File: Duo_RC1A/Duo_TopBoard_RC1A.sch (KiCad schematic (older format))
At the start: 32 parts, among them CN1 CONN_PANNEL_2X2, CN2 CONN_PANNEL_2X2, P1 PIN_ARRAY_2X10, P2 KK3.96_2, Q1 MMBT3904, Q2 MMBT3904

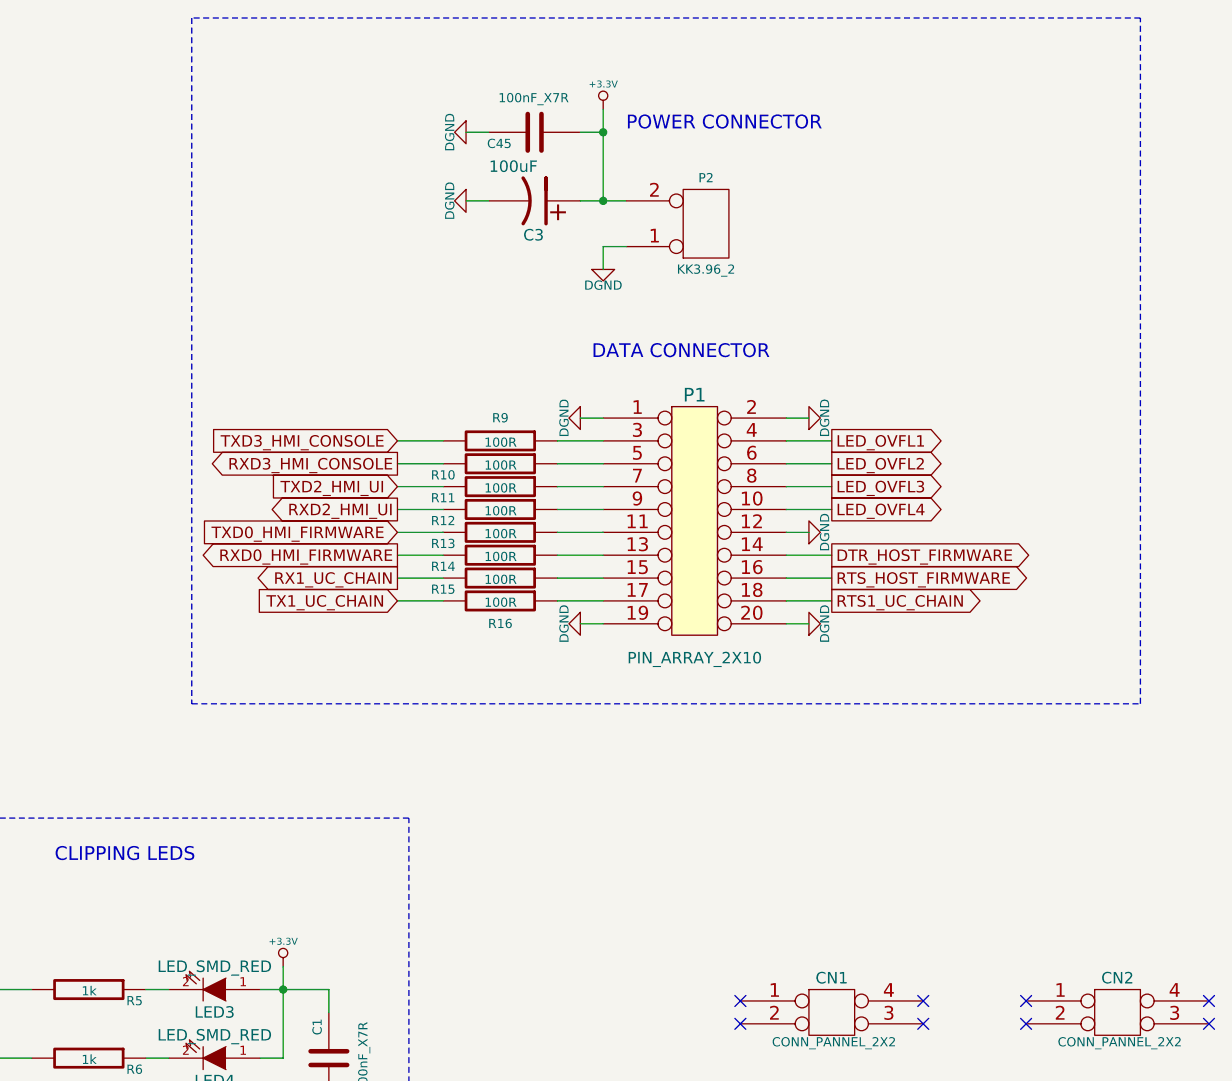
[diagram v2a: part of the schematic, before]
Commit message: Removed CODEC_MITEC signal. Defined the connector between the TopBoard and the BottomBoard. Saved layouts in *.brd old format.
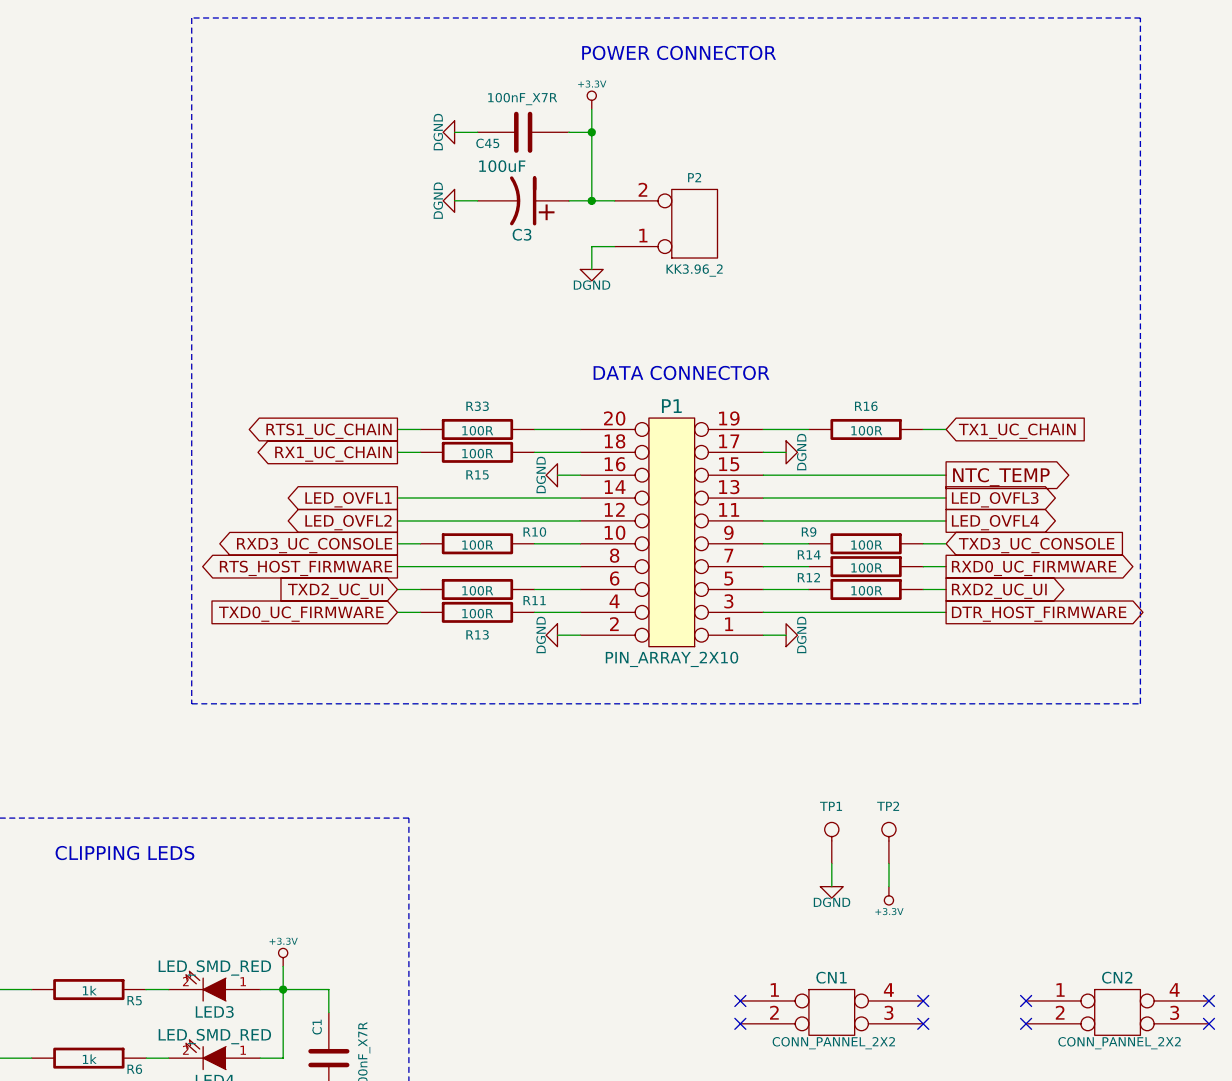
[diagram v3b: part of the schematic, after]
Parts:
- added R33: 100R, Duo_Audio_HMI_RC1A:SM0603, symbol R
- added TP1: CONN_1, Duo_Audio_HMI_RC1A:TESTPOINT_2.2MM, symbol CONN_1
- added TP2: CONN_1, Duo_Audio_HMI_RC1A:TESTPOINT_1MM, symbol CONN_1
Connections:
- net RXD0_HMI_FIRMWARE is gone; now on an unnamed net: R14.2
- net RXD2_HMI_UI is gone; now on an unnamed net: R12.2
- net TXD3_HMI_CONSOLE is gone; now on an unnamed net: R9.2
- net +3.3V: now also TP2.1
- net DGND: now also P1.16 (P16), P1.17 (P17), TP1.1; no longer P1.12 (P12), P1.19 (P19), P1.20 (P20)
- net DTR_HOST_FIRMWARE: now also P1.3 (P3); no longer P1.14 (P14)
- net LED_OVFL1: now also P1.14 (P14); no longer P1.4 (P4)
- net LED_OVFL2: now also P1.12 (P12); no longer P1.6 (P6)
- net LED_OVFL3: now also P1.13 (P13); no longer P1.8 (P8)
- net LED_OVFL4: now also P1.11 (P11); no longer P1.10 (P10)
- net RTS1_UC_CHAIN: now also R33.1; no longer P1.18 (P18)
- net RTS_HOST_FIRMWARE: now also P1.8 (P8); no longer P1.16 (P16)
- net RX1_UC_CHAIN: now also R15.1; no longer R15.2
- net TX1_UC_CHAIN: now also R16.1; no longer R16.2
- net TXD3_UC_CONSOLE: now reaches R9.1
- net TXD3_UC_CONSOLE: no longer P1.3 (P3)
- net at P1.5 (P5): no longer R10.1
- net at P1.7 (P7): no longer R11.1
- net at P1.9 (P9): no longer R12.1
- net TXD0_UC_FIRMWARE: now reaches R13.1
- net TXD0_UC_FIRMWARE: no longer P1.11 (P11)
- net RXD0_UC_FIRMWARE: now reaches R14.1
- net RXD0_UC_FIRMWARE: no longer P1.13 (P13)
- net NTC_TEMP: now reaches P1.15 (P15)
- net NTC_TEMP: no longer R15.1
- net RXD3_HMI_CONSOLE: no longer names the net of R10.2
- net RXD3_HMI_CONSOLE: now also P1.10 (P10)
- net TXD0_HMI_FIRMWARE: no longer names the net of R13.2
- net TXD0_HMI_FIRMWARE: now also P1.4 (P4)
- net TXD2_HMI_UI: no longer names the net of R11.2
- net TXD2_HMI_UI: now also P1.6 (P6)
- new net: P1.18 (P18), R15.2
- new net: P1.19 (P19), R16.2
- new net: P1.20 (P20), R33.2
- new net RXD2_UC_UI: R12.1
- new net RXD3_UC_CONSOLE: R10.1
- new net TXD2_UC_UI: R11.1
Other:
- moved on the sheet: C3, C45, P1, P2, R10, R11, R12, R13, R14, R15, R16, R9

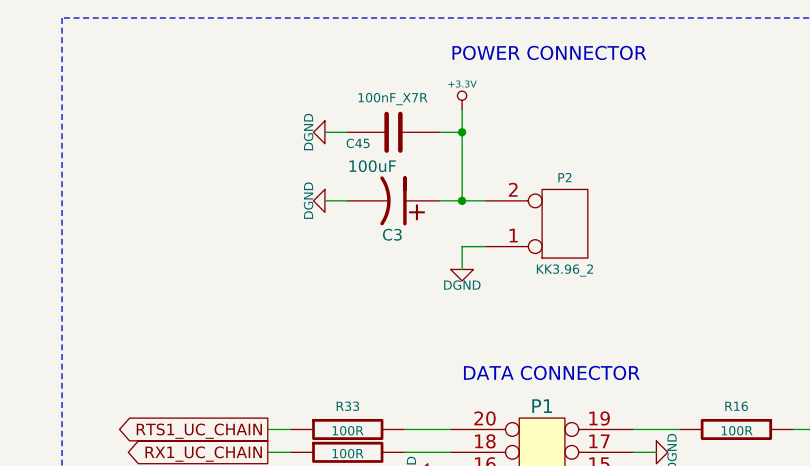
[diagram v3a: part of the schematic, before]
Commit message: Finished the TopBoard layout.
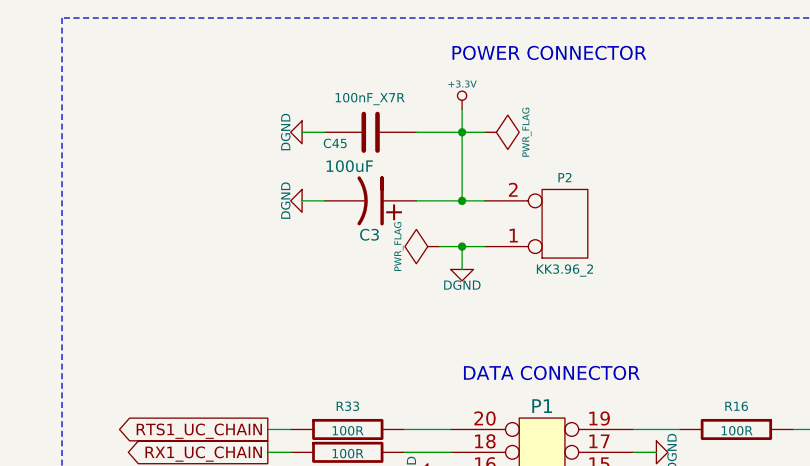
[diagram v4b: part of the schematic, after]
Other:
- moved on the sheet: C3, C45
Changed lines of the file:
@@
 L CP1 C3
 U 1 1 537BE552
-P 7100 2100
-F 0 "C3" V 6950 2050 50  0000 L CNN
-F 1 "100uF" V 7250 1900 50  0000 L CNN
-F 2 "Duo_Audio_HMI_RC1A:Capacitor5x11RM2" H 7100 2100 60  0001 C CNN
-F 3 "" H 7100 2100 60  0000 C CNN
-	1    7100 2100
+P 7000 2100
+F 0 "C3" V 6850 2050 50  0000 L CNN
+F 1 "100uF" V 7150 1900 50  0000 L CNN
+F 2 "Duo_Audio_HMI_RC1A:Capacitor5x11RM2" H 7000 2100 60  0001 C CNN
+F 3 "" H 7000 2100 60  0000 C CNN
+	1    7000 2100
 	0    1    -1   0
 $EndComp
@@
 L DGND #PWR06
 U 1 1 537BE5A7
-P 6800 2100
-F 0 "#PWR06" H 6800 2100 40  0001 C CNN
-F 1 "DGND" H 6800 2030 40  0000 C CNN
-F 2 "" H 6800 2100 60  0000 C CNN
-F 3 "" H 6800 2100 60  0000 C CNN
-	1    6800 2100
+P 6700 2100
+F 0 "#PWR06" H 6700 2100 40  0001 C CNN
+F 1 "DGND" H 6700 2030 40  0000 C CNN
+F 2 "" H 6700 2100 60  0000 C CNN
+F 3 "" H 6700 2100 60  0000 C CNN
+	1    6700 2100
 	0    1    1    0
 $EndComp
@@
 L C C45
 U 1 1 538344CA
-P 7100 1800
-F 0 "C45" V 7050 1900 40  0000 L CNN
-F 1 "100nF_X7R" V 7250 1650 40  0000 L CNN
-F 2 "Duo_Audio_HMI_RC1A:SM0603" H 7138 1650 30  0001 C CNN
-F 3 "" H 7100 1800 60  0000 C CNN
-	1    7100 1800
+P 7000 1800
+F 0 "C45" V 6950 1900 40  0000 L CNN
+F 1 "100nF_X7R" V 7150 1650 40  0000 L CNN
+F 2 "Duo_Audio_HMI_RC1A:SM0603" H 7038 1650 30  0001 C CNN
+F 3 "" H 7000 1800 60  0000 C CNN
+	1    7000 1800
 	0    -1   -1   0
 $EndComp
@@
 L DGND #PWR017
 U 1 1 53834546
-P 6800 1800
-F 0 "#PWR017" H 6800 1800 40  0001 C CNN
-F 1 "DGND" H 6800 1730 40  0000 C CNN
-F 2 "" H 6800 1800 60  0000 C CNN
-F 3 "" H 6800 1800 60  0000 C CNN
-	1    6800 1800
+P 6700 1800
+F 0 "#PWR017" H 6700 1800 40  0001 C CNN
+F 1 "DGND" H 6700 1730 40  0000 C CNN
+F 2 "" H 6700 1800 60  0000 C CNN
+F 3 "" H 6700 1800 60  0000 C CNN
+	1    6700 1800
 	0    1    1    0
 $EndComp
@@
 	7400 1700 7400 2100
 Wire Wire Line
-	7300 2100 7500 2100
-Wire Wire Line
-	7500 2300 7400 2300
+	7200 2100 7500 2100
+Wire Wire Line
+	7300 2300 7500 2300
 Wire Wire Line
 	7400 2300 7400 2400
@@
 Connection ~ 7400 2100
 Wire Wire Line
-	6800 2100 6900 2100
+	6700 2100 6800 2100
 Wire Wire Line
 	1950 5450 2150 5450
@@
 	9800 1300 5650 1300
 Wire Wire Line
-	7300 1800 7400 1800
+	7200 1800 7500 1800
 Connection ~ 7400 1800
 Wire Wire Line
-	6800 1800 6900 1800
+	6700 1800 6800 1800
 Wire Wire Line
 	7350 3200 7150 3200
@@
 Wire Wire Line
 	8700 5000 8700 5100
+$Comp
+L PWR_FLAG #FLG021
+U 1 1 538C7AA6
+P 7500 1800
+F 0 "#FLG021" H 7500 1895 30  0001 C CNN
+F 1 "PWR_FLAG" H 7500 1980 30  0000 C CNN
+F 2 "" H 7500 1800 60  0000 C CNN
+F 3 "" H 7500 1800 60  0000 C CNN
+	1    7500 1800
+	0    1    1    0
+$EndComp
+$Comp
+L PWR_FLAG #FLG022
+U 1 1 538C7B17
+P 7300 2300
+F 0 "#FLG022" H 7300 2395 30  0001 C CNN
+F 1 "PWR_FLAG" H 7300 2480 30  0000 C CNN
+F 2 "" H 7300 2300 60  0000 C CNN
+F 3 "" H 7300 2300 60  0000 C CNN
+	1    7300 2300
+	0    -1   -1   0
+$EndComp
+Connection ~ 7400 2300
 $EndSCHEMATC

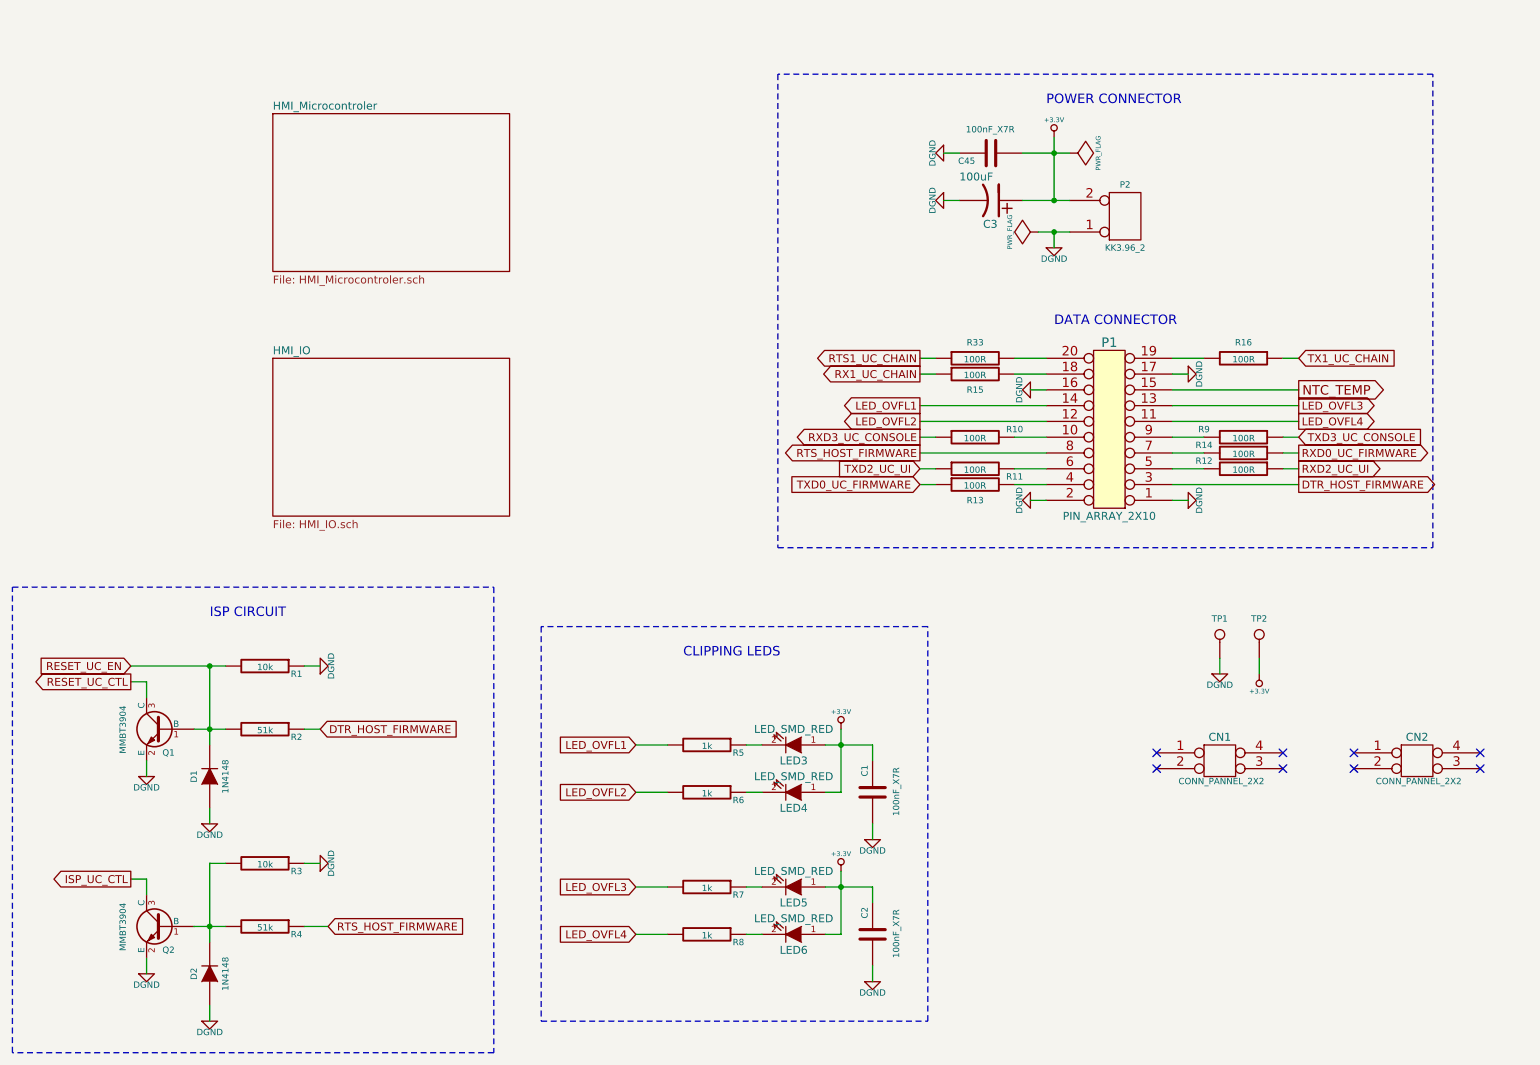
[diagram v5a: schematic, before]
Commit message: Changed the LCD for the 2.8pol. Rotated the bottom board connector. Moved the 3.3V linear regulator from the bottom board to the top board, and changed the power for the top board from 3.3V to 9V.
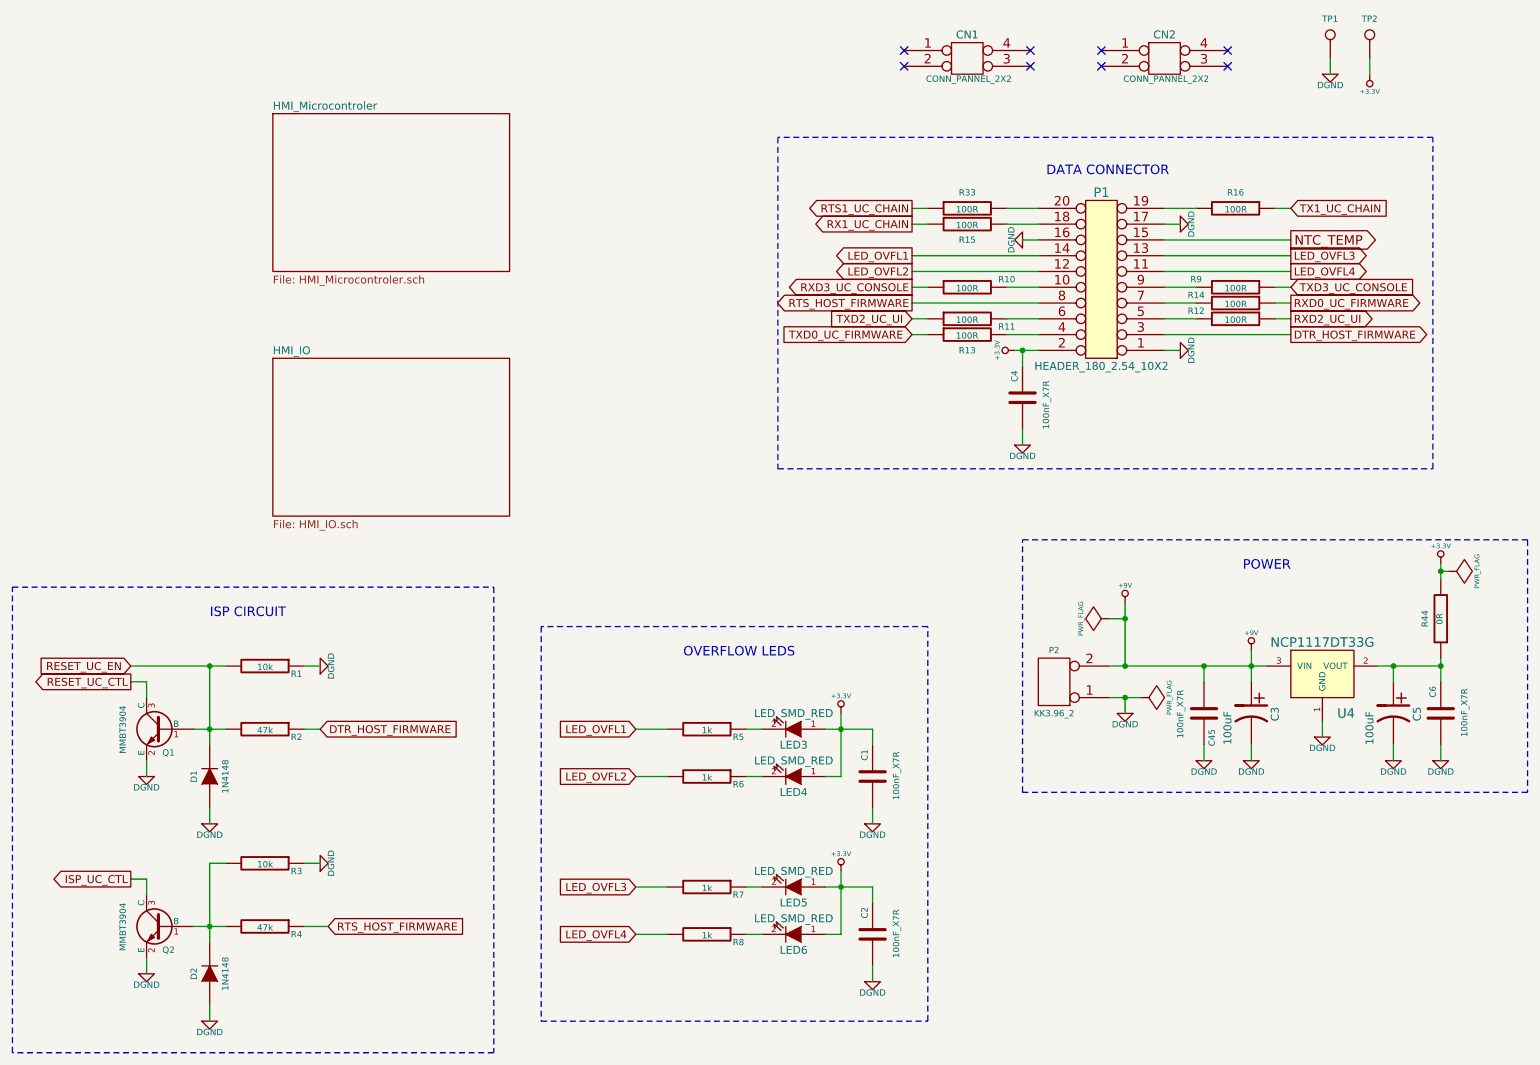
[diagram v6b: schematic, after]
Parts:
- added C4, C6: 100nF_X7R, Duo_Audio_HMI_RC1A:SM0603, symbol C
- added C5: 100uF, Duo_Audio_HMI_RC1A:Capacitor5x11RM2, symbol CP1
- added R44: 0R, Duo_Audio_HMI_RC1A:SM0805, symbol R
- added U4: NCP1117DT33G, Duo_Audio_HMI_RC1A:DPAK(369C), symbol NCP1117DT33G
- P1: value PIN_ARRAY_2X10 -> HEADER_180_2.54_10X2
- R2, R4: value 51k -> 47k
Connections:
- net +3.3V: now also P1.2 (P2), C4.1, R44.2; no longer C3.1, C45.2, P2.2 (PM)
- net DGND: now also C4.2, C5.2, C6.2, U4.1 (GND); no longer P1.2 (P2)
- new net: C5.1, C6.1, R44.1, U4.2 (VOUT)
- new net +9V: C3.1, C45.2, P2.2 (PM), U4.3 (VIN)
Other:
- note added: "OVERFLOW LEDS"
- note added: "POWER"
- note removed: "CLIPPING LEDS"
- note removed: "POWER CONNECTOR"
- moved on the sheet: C1, C3, C45, CN1, CN2, LED3, LED4, P1, P2, R10, R11, R12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
